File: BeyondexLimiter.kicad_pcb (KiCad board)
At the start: 2 copper layers, 22.5 x 13 mm, 8 parts, among them U1 MIC2544-1YM

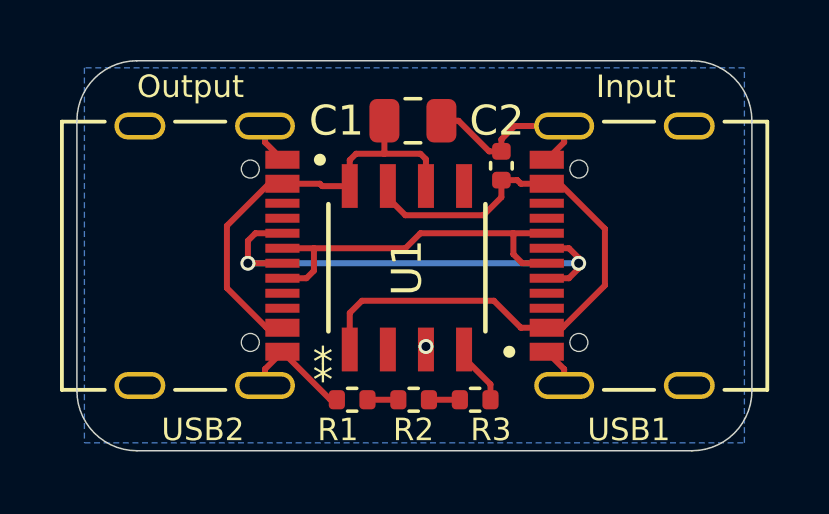
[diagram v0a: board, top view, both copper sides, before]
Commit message: Simplify to 2 resistors and add THT customization
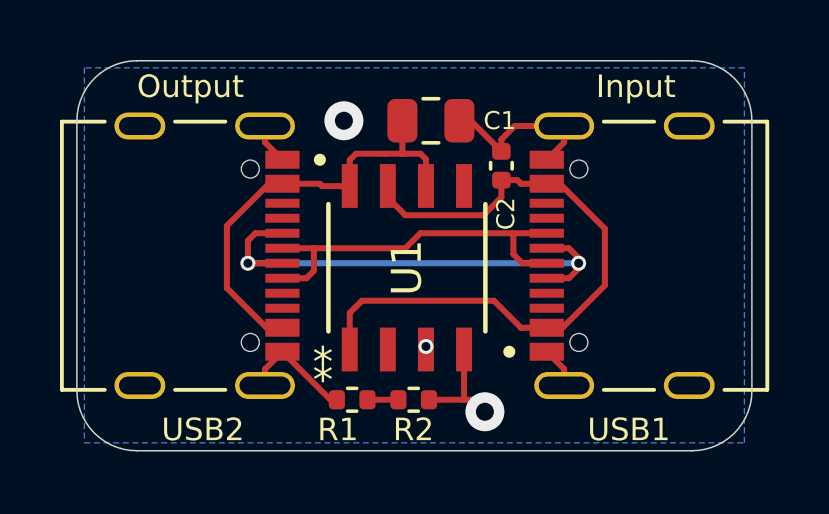
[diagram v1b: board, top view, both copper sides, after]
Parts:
- removed R3: 680Ω ±1%, Resistor_SMD:R_0402_1005Metric
- R1: value 150Ω ±1% -> 1kΩ ±1%
- R2: value 330Ω ±1% -> 150Ω ±1%
- moved C1 0.60 mm to (169.3, 93.0)
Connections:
- R2 pad 1: Net-(R2-Pad1) -> Net-(U1-ILIM)
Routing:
- net Net-(U1-ILIM): track 2.04 -> 3.71 mm, vias 0 -> 1
- net Net-(R2-Pad1): track 1.03 -> 0.00 mm
- net GND: track 13.0 -> 12.4 mm, vias 1 -> 2

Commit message: Bump version
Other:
- board text added: "Beyondex Current Limiter USB 2.0 200mA Limit v0.3 Designed by Kibbie"
- board text removed: "Beyondex Current Limiter USB 2.0 200mA Limit v0.2 Designed by Kibbie"
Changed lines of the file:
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@@
 		)
 	)
-	(gr_text "Beyondex Current Limiter\nUSB 2.0 200mA Limit\nv0.2 Designed by Kibbie"
+	(gr_text "Beyondex Current Limiter\nUSB 2.0 200mA Limit\nv0.3 Designed by Kibbie"
 		(at 168.8 97.5 0)
 		(layer "B.SilkS")

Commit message: Adjust back silkscreen to better accommodate mounting holes
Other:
- board text added: "Beyondex Current Limiter USB 2.0 200mA Limit v0.4 Designed by Kibbie"
- board text added: "Out→"
- board text added: "→In"
- board text removed: "Beyondex Current Limiter USB 2.0 200mA Limit v0.3 Designed by Kibbie"
- board text removed: "Input Upstream"
- board text removed: "Output Downstream"
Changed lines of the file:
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@@
 		)
 	)
-	(gr_text "Beyondex Current Limiter\nUSB 2.0 200mA Limit\nv0.3 Designed by Kibbie"
+	(gr_text "→In"
+		(at 179.9 97.5 0)
+		(layer "B.SilkS")
+		(effects
+			(font
+				(size 0.75 0.75)
+				(thickness 0.09375)
+				(bold yes)
+			)
+			(justify left mirror)
+		)
+	)
+	(gr_text "Beyondex Current Limiter\nUSB 2.0 200mA Limit\nv0.4 Designed by Kibbie"
 		(at 168.8 97.5 0)
 		(layer "B.SilkS")
@@
 		)
 	)
-	(gr_text "Output\nDownstream"
-		(at 160 97.5 90)
+	(gr_text "Out→"
+		(at 157.7 97.5 0)
 		(layer "B.SilkS")
 		(effects
@@
 				(thickness 0.1)
 			)
-			(justify bottom mirror)
+			(justify right mirror)
 		)
 	)
-	(gr_text "Input\nUpstream"
-		(at 177.6 97.5 270)
-		(layer "B.SilkS")
-		(effects
-			(font
-				(size 0.75 0.75)
-				(thickness 0.1)
-			)
-			(justify bottom mirror)
-		)
-	)

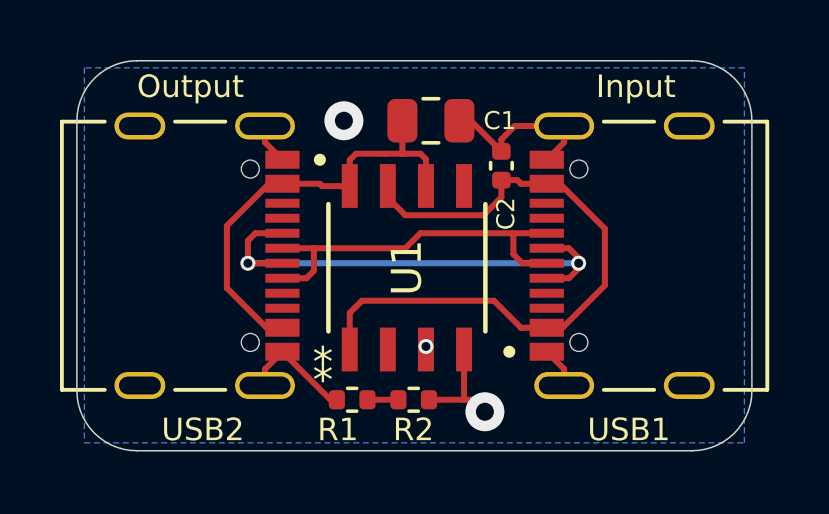
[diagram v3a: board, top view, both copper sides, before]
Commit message: Replace MIC2544 with SGM2523A for faster response
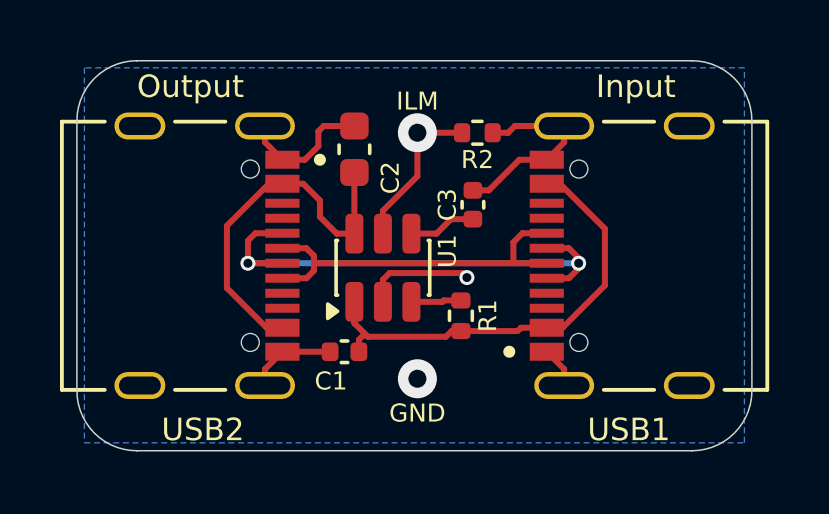
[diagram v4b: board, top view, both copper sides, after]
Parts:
- removed the R2 at (168.7, 102.3)
- added C3: 1.2nF, Capacitor_SMD:C_0402_1005Metric, F.Cu at (170.7, 95.8)
- added R1: 1kΩ ±1%, Resistor_SMD:R_0402_1005Metric, F.Cu at (170.3, 99.5)
- C1: renamed from C2; value 100nF -> 10uF
- C2: renamed from C1; value 33uF -> 2.2uF; footprint Capacitor_SMD:C_0805_2012Metric -> Capacitor_SMD:C_0603_1608Metric
- R2: renamed from R1; value 1kΩ ±1% -> 10kΩ ±1%
- U1: value MIC2544-1YM -> SGM2523; footprint BeyondexLimiter:SOIC-8_M_MCL -> Package_TO_SOT_SMD:SOT-23-6
- moved R2 9.83 mm to (170.8, 93.4)
- moved C1 8.11 mm to (166.4, 100.7), turned to 180 degrees
- moved C2 2.72 mm to (166.8, 94.0), turned to 90 degrees
- moved U1 0.80 mm to (167.7, 97.9)
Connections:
- R2 pad 1: Net-(R1-Pad1) -> GND
- R2 pad 2: GND -> /ILM
- U1 pad 2: unconnected-(U1-FLG-Pad2) -> GND
- U1 pad 3: GND -> Net-(U1-ENFLT)
- U1 pad 4: Net-(U1-ILIM) -> /SS
- U1 pad 5: unconnected-(U1-NC-Pad5) -> /ILM
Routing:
- net /VIN: track 22.1 -> 15.1 mm
- net GND: track 12.4 -> 19.4 mm
- net /ILM: track 0.00 -> 5.33 mm, vias 0 -> 1
- net Net-(U1-ILIM): track 3.71 -> 0.00 mm, vias 1 -> 0
- net /VOUT: track 14.7 -> 12.3 mm
- net /SS: track 0.00 -> 2.25 mm
- net Net-(U1-ENFLT): track 0.00 -> 1.67 mm
- net Net-(R1-Pad1): track 1.03 -> 0.00 mm
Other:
- board text added: "Beyondex Current Limiter USB 2.0 100mA Limit v0.5 Designed by Kibbie"
- board text added: "GND"
- board text added: "ILM"
- board text removed: "Beyondex Current Limiter USB 2.0 200mA Limit v0.4 Designed by Kibbie"

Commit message: Slight reorganization of components, add SGM2523 datasheet
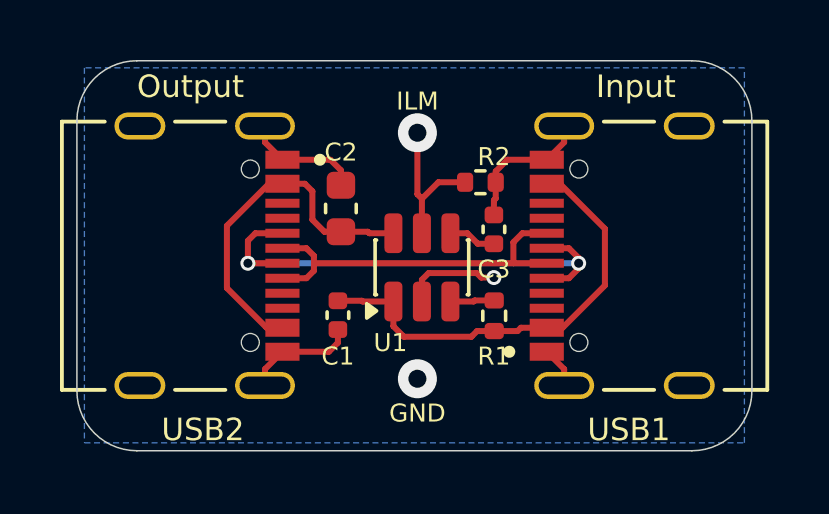
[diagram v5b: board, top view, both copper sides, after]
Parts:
- moved C2 2.03 mm to (166.3, 95.9)
- moved R2 1.65 mm to (170.9, 95.0)
- moved U1 1.30 mm to (169.0, 97.9)
- moved C1 1.24 mm to (166.2, 99.5), turned to -90 degrees
- moved R1 1.11 mm to (171.4, 99.5)
- moved C3 1.08 mm to (171.4, 96.6)
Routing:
- net GND: track 19.4 -> 17.2 mm
- net /SS: track 2.25 -> 1.59 mm
- net /VOUT: track 12.3 -> 11.8 mm

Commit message: Slight component adjustments
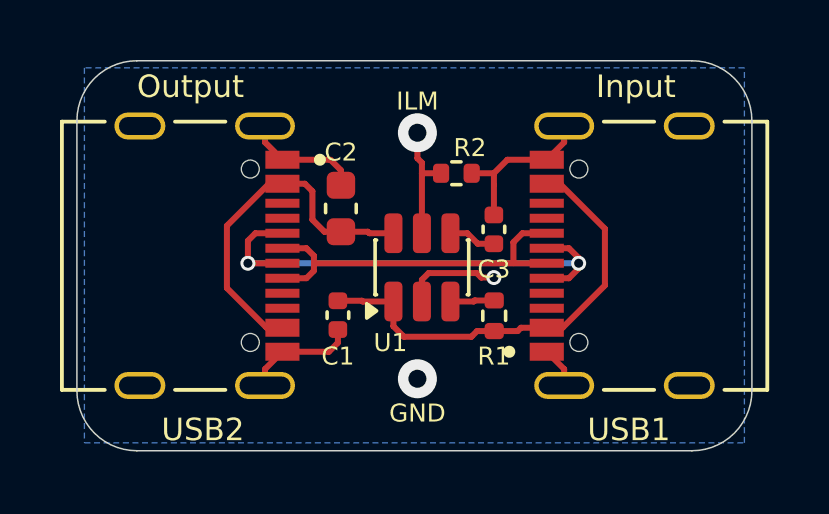
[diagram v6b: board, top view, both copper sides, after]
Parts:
- moved R2 0.85 mm to (170.2, 94.8)
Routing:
- net /ILM: track 5.08 -> 4.05 mm
- net GND: track 17.2 -> 18.0 mm
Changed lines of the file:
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@@
 	(footprint "Resistor_SMD:R_0402_1005Metric"
 		(layer "F.Cu")
-		(at 170.95 95.05 180)
+		(at 170.15 94.75 180)
 		(descr "Resistor SMD 0402 (1005 Metric), square (rectangular) end terminal, IPC-7351 nominal, (Body size source: IPC-SM-782 page 72, https://www.pcb-3d.com/wordpress/wp-content/uploads/ipc-sm-782a_amendment_1_and_2.pdf), generated with kicad-footprint-generator")
 		(tags "resistor")
@@
 	)
 	(segment
-		(start 171.46 94.69)
-		(end 171.46 95.05)
-		(width 0.2)
-		(layer "F.Cu")
-		(net 1)
-	)
-	(segment
-		(start 171.46 95.59)
-		(end 171.4 95.65)
+		(start 173.1625 94.3)
+		(end 171.85 94.3)
+		(width 0.2)
+		(layer "F.Cu")
+		(net 1)
+	)
+	(segment
+		(start 171.4 95.15)
+		(end 171.4 96.14)
 		(width 0.2)
 		(layer "F.Cu")
@@
 	)
 	(segment
+		(start 171.4 94.75)
+		(end 171.4 95.15)
+		(width 0.2)
+		(layer "F.Cu")
+		(net 1)
+	)
+	(segment
 		(start 163.77 101.28)
 		(end 164.35 100.7)
@@
 	)
 	(segment
-		(start 171.46 95.05)
-		(end 171.46 95.59)
-		(width 0.2)
-		(layer "F.Cu")
-		(net 1)
-	)
-	(segment
 		(start 173.7425 93.72)
 		(end 173.1625 94.3)
@@
 	)
 	(segment
+		(start 171.85 94.3)
+		(end 171.4 94.75)
+		(width 0.2)
+		(layer "F.Cu")
+		(net 1)
+	)
+	(segment
 		(start 169 98.3)
 		(end 169 99.025)
@@
 	)
 	(segment
-		(start 173.1625 94.3)
-		(end 171.85 94.3)
-		(width 0.2)
-		(layer "F.Cu")
-		(net 1)
-	)
-	(segment
-		(start 171.85 94.3)
-		(end 171.46 94.69)
-		(width 0.2)
-		(layer "F.Cu")
-		(net 1)
-	)
-	(segment
 		(start 163.77 93.72)
 		(end 164.35 94.3)
@@
 	)
 	(segment
+		(start 171.4 94.75)
+		(end 170.66 94.75)
+		(width 0.2)
+		(layer "F.Cu")
+		(net 1)
+	)
+	(segment
 		(start 166.2 100.4)
 		(end 166.2 99.96)
-		(width 0.2)
-		(layer "F.Cu")
-		(net 1)
-	)
-	(segment
-		(start 171.4 95.65)
-		(end 171.4 96.14)
 		(width 0.2)
 		(layer "F.Cu")
@@
 	)
 	(segment
-		(start 169.55 95.05)
-		(end 169 95.6)
+		(start 169 94.75)
+		(end 169 96.75)
 		(width 0.2)
 		(layer "F.Cu")
@@
 	(segment
 		(start 168.85 93.4)
-		(end 168.85 95.45)
+		(end 168.85 94.25)
 		(width 0.2)
 		(layer "F.Cu")
@@
 	)
 	(segment
-		(start 168.85 95.45)
-		(end 169 95.6)
+		(start 169 94.4)
+		(end 169 94.75)
 		(width 0.2)
 		(layer "F.Cu")
@@
 	)
 	(segment
-		(start 169 95.6)
-		(end 169 96.75)
+		(start 168.85 94.25)
+		(end 169 94.4)
 		(width 0.2)
 		(layer "F.Cu")
@@
 	)
 	(segment
-		(start 170.44 95.05)
-		(end 169.55 95.05)
-		(width 0.2)
-		(layer "F.Cu")
+		(start 169.64 94.75)
+		(end 169 94.75)
+		(width 0.2)
+		(layer "F.Cu")

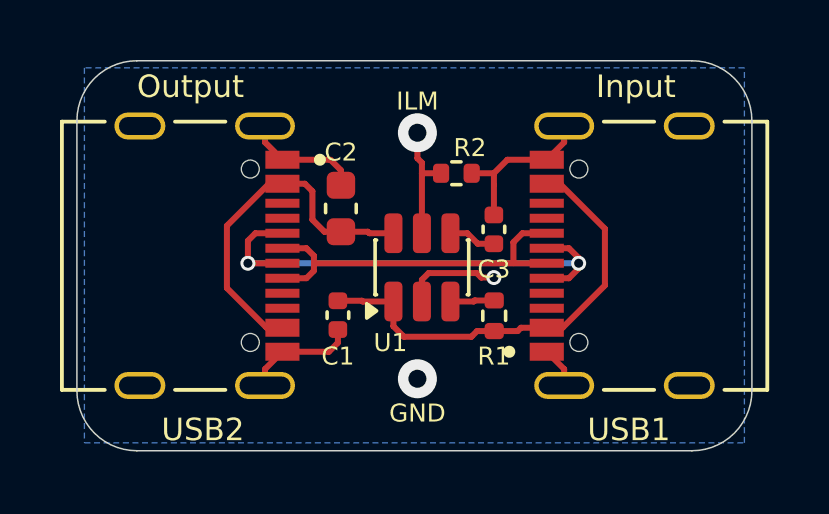
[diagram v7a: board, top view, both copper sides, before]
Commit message: Remake limiter with CN5711 and adjustable limit
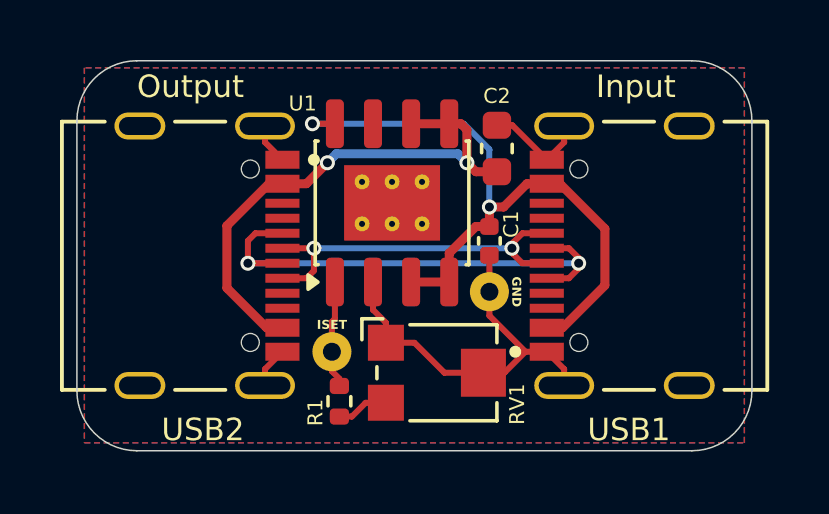
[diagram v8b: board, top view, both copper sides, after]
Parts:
- removed C3: 1.2nF, Capacitor_SMD:C_0402_1005Metric
- removed R2: 10kΩ ±1%, Resistor_SMD:R_0402_1005Metric
- added RV1: R_Potentiometer, Potentiometer_SMD:Potentiometer_Bourns_TC33X_Vertical, F.Cu at (169.6, 101.4)
- added TP1: ISET, BeyondexLimiter:TestPoint_Plated_Hole_D0.6mm, F.Cu at (166.0, 100.7)
- added TP2: GND, BeyondexLimiter:TestPoint_Plated_Hole_D0.6mm, F.Cu at (171.2, 98.7)
- R1: value 1kΩ ±1% -> 3.6kΩ ±1%
- U1: value SGM2523 -> CN5711; footprint Package_TO_SOT_SMD:SOT-23-6 -> Package_SO:SOIC-8-1EP_3.9x4.9mm_P1.27mm_EP2.514x3.2mm_ThermalVias
- moved R1 5.89 mm to (166.2, 102.3)
- moved C1 5.62 mm to (171.2, 97.0)
- moved C2 5.57 mm to (171.5, 93.9)
- moved U1 2.37 mm to (168.0, 95.7)
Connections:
- R1 pad 1: Net-(U1-ENFLT) -> /ISET
- R1 pad 2: /VIN -> Net-(R1-Pad2)
- U1 pad 1: /VIN -> /ISET
- U1 pad 3: Net-(U1-ENFLT) -> /VIN
- U1 pad 4: /SS -> /VIN
- U1 pad 5: /ILM -> /VOUT
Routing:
- net /VIN: track 15.0 -> 22.7 mm, vias 0 -> 2
- net /VOUT: track 11.8 -> 17.8 mm, vias 0 -> 2
- net /ILM: track 4.05 -> 0.00 mm, vias 1 -> 0
- net /ISET: track 0.00 -> 3.61 mm
- net Net-(R1-Pad2): track 0.00 -> 1.74 mm
- net GND: track 18.0 -> 19.6 mm, vias 2 -> 0
- net /SS: track 1.59 -> 0.00 mm
- net Net-(U1-ENFLT): track 1.47 -> 0.00 mm
- net /D+: track 12.5 -> 12.7 mm, vias 0 -> 2
- added copper zone on F.Cu, net GND
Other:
- board text added: "Beyondex Current Limiter USB 2.0 Adjustable Limit v0.6 Designed by Kibbie"
- board text removed: "Beyondex Current Limiter USB 2.0 100mA Limit v0.5 Designed by Kibbie"
- board text removed: "GND"
- board text removed: "ILM"
